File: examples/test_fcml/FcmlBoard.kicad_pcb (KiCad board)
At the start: 2 copper layers, 139 x 123 mm, 160 parts

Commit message: Update FcmlBoard.kicad_pcb
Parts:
- moved cdone.package 58.0 mm to (-35.0, 135.0), turned to 0 degrees
- moved cdone.res 56.7 mm to (-35.0, 137.0)
- moved fpga.vio_cap2 27.5 mm to (-35.0, 123.0), turned to 180 degrees
- moved fpga.vpp_cap 24.7 mm to (-21.0, 135.0)
- moved fpga.pll_hf 24.5 mm to (-25.0, 135.0)
- moved fpga.vio_cap1 20.5 mm to (-21.0, 137.0)
- moved fpga.pll_lf 20.2 mm to (-25.0, 139.0)
- moved fpga.vcc_cap 19.5 mm to (-35.0, 125.0), turned to 180 degrees
- moved fpga.vio_cap0 18.3 mm to (-25.0, 125.0), turned to 180 degrees
- moved fpga.reset_pu 16.5 mm to (-39.2, 151.0)
- moved fpga.pll_res 15.8 mm to (-25.0, 137.0), turned to 180 degrees
- moved fpga.mem_pu 6.42 mm to (-33.0, 154.0)

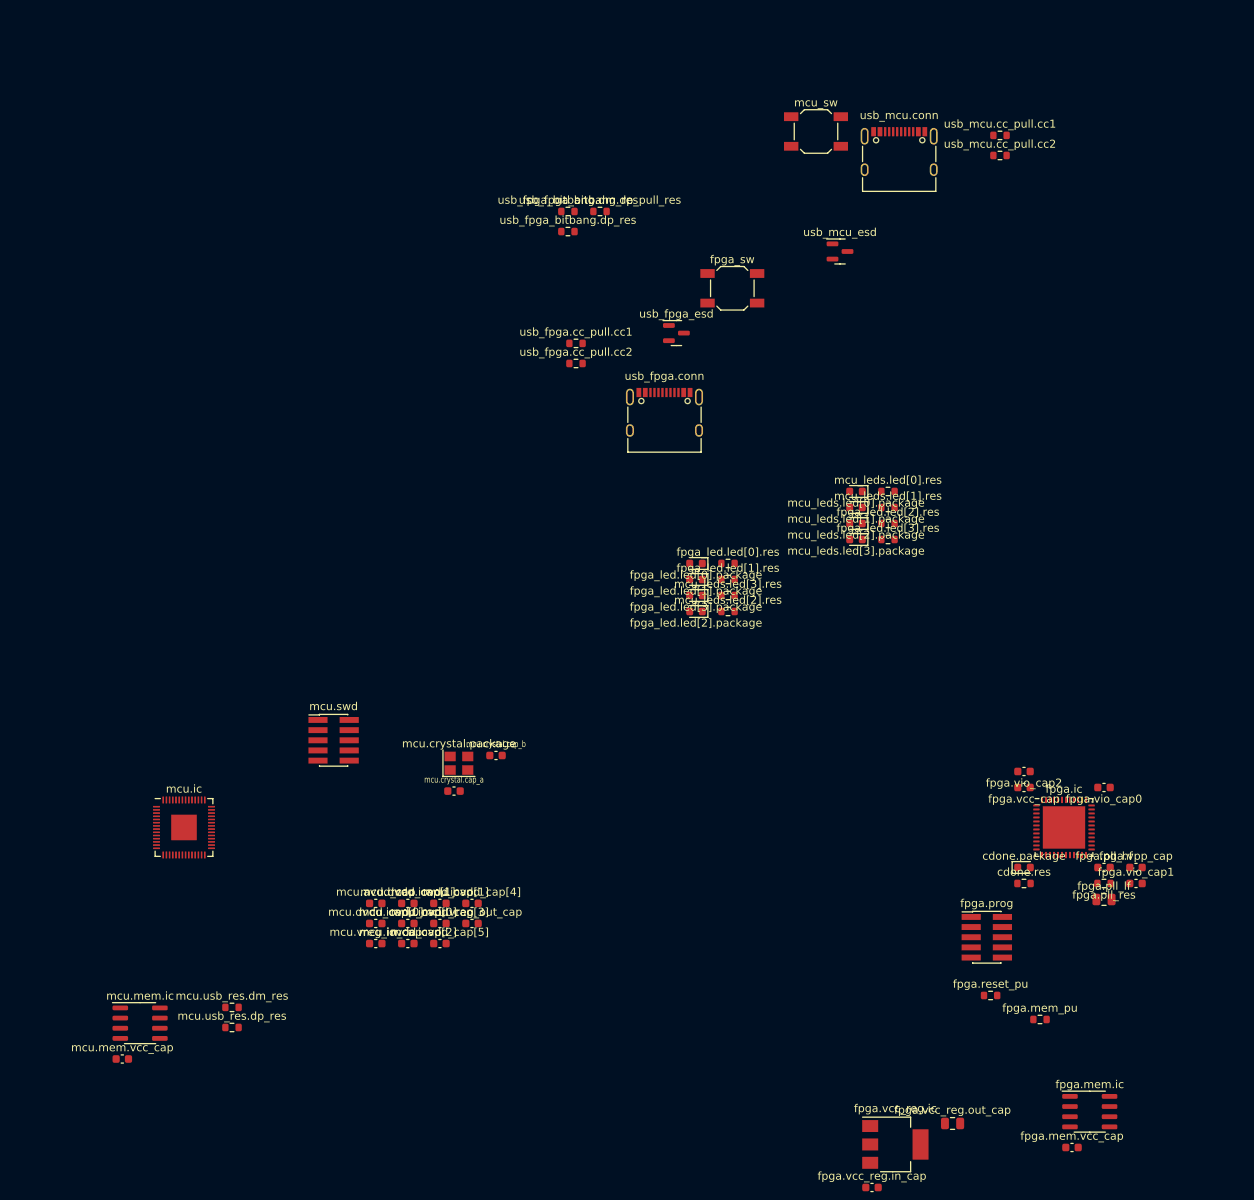
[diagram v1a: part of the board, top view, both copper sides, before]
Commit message: fpga and micro subckt routing
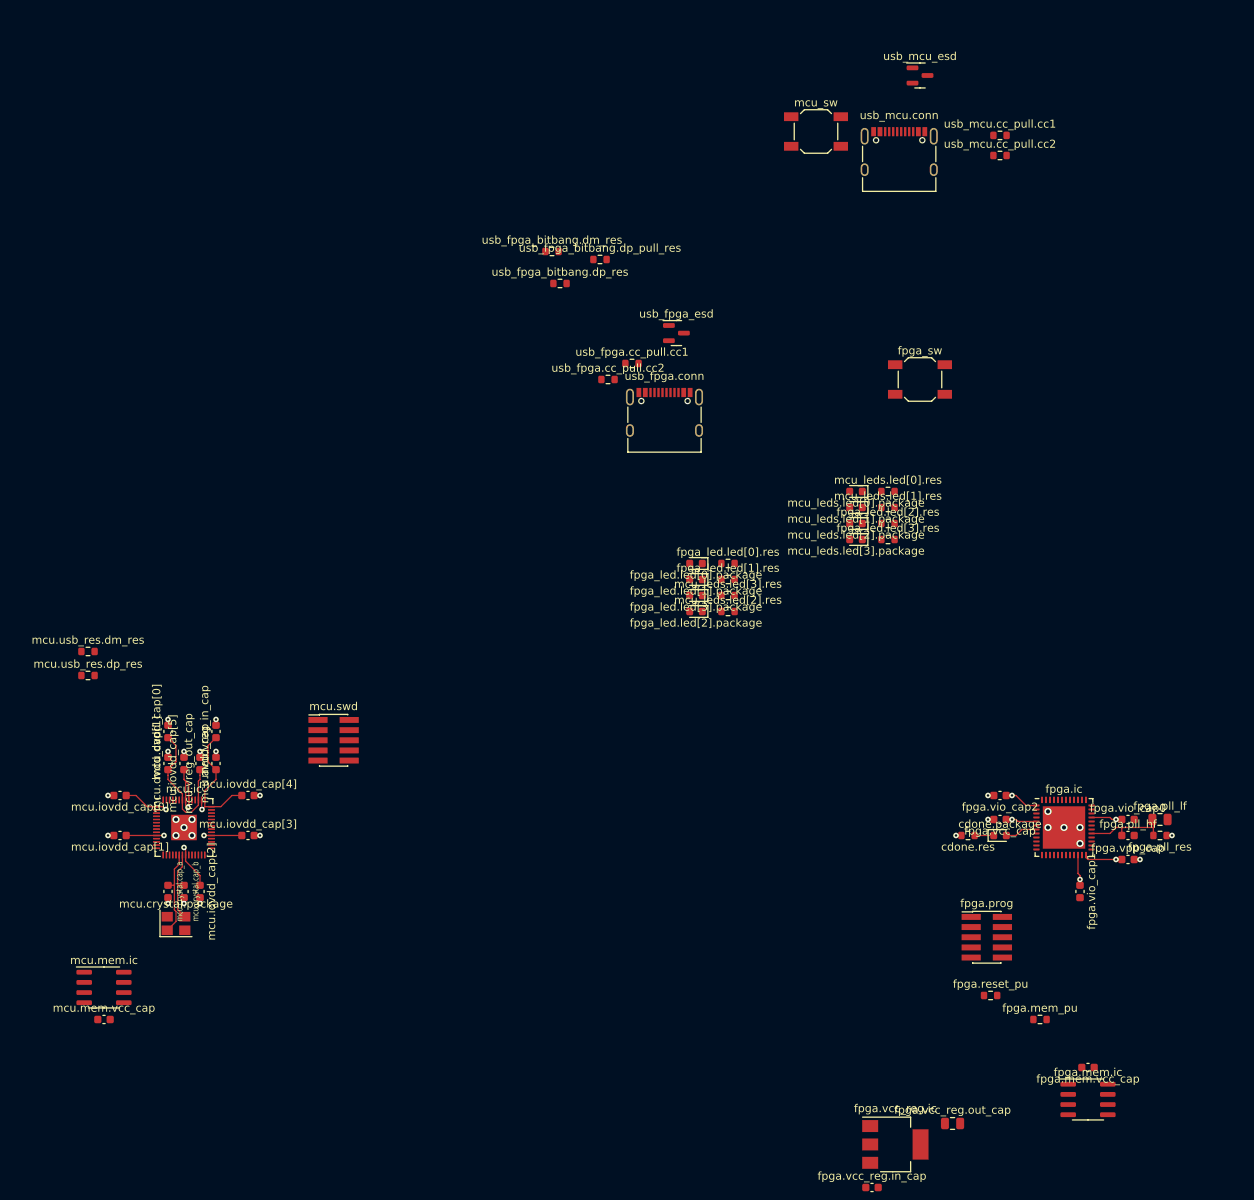
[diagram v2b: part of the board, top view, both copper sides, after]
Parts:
- moved mcu.usb_res.dm_res 48.0 mm to (-152.0, 108.0)
- moved mcu.usb_res.dp_res 47.5 mm to (-152.0, 111.0)
- moved mcu.crystal.cap_b 42.5 mm to (-140.0, 138.0), turned to -90 degrees
- moved mcu.iovdd_cap[1] 40.9 mm to (-148.0, 131.0), turned to 180 degrees
- moved mcu.crystal.package 40.6 mm to (-141.0, 142.0)
- moved mcu.vreg_out_cap 39.4 mm to (-138.0, 122.0), turned to 90 degrees
- moved mcu.iovdd_cap[0] 39.4 mm to (-148.0, 126.0), turned to 180 degrees
- moved mcu.iovdd_cap[5] 39.1 mm to (-140.0, 122.0), turned to 90 degrees
- moved mcu.crystal.cap_a 37.9 mm to (-142.0, 138.0), turned to -90 degrees
- moved mcu.dvdd_cap[0] 35.4 mm to (-142.0, 118.0), turned to 90 degrees
- moved mcu.dvdd_cap[1] 34.7 mm to (-142.0, 122.0), turned to 90 degrees
- moved mcu.vreg_in_cap 33.2 mm to (-136.0, 118.0), turned to 90 degrees
- moved mcu.iovdd_cap[4] 31.1 mm to (-132.0, 126.0)
- moved mcu.iovdd_cap[2] 26.8 mm to (-138.0, 138.0), turned to -90 degrees
- moved mcu.avdd_cap 26.5 mm to (-136.0, 122.0), turned to 90 degrees
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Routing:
- net v3v3: track 45.7 -> 110.4 mm, vias 4 -> 14
- net gnd: track 30.5 -> 58.1 mm, vias 22 -> 49
- net mcu.ic.vreg_vout: track 0.00 -> 17.5 mm
- net fpga.pll_res.pwr_out: track 0.00 -> 11.1 mm
- net mcu.crystal.crystal.a: track 0.00 -> 11.0 mm
- net mcu.crystal.crystal.b: track 0.00 -> 9.14 mm
- net fpga.vcc_reg.pwr_out: track 0.00 -> 5.28 mm, vias 0 -> 2
- net fpga.cdone: track 0.00 -> 4.07 mm
- net cdone.res.a: track 0.00 -> 2.39 mm

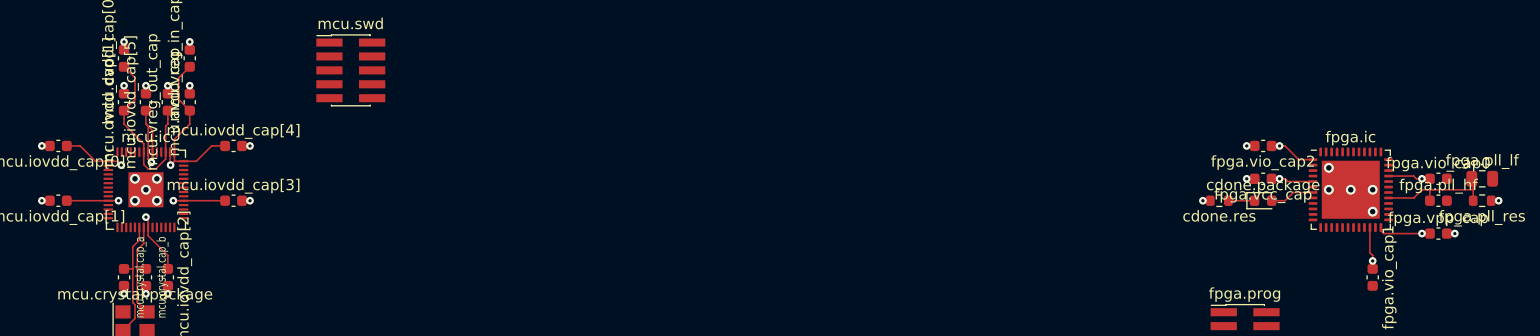
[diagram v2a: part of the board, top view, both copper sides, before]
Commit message: thicker power traces
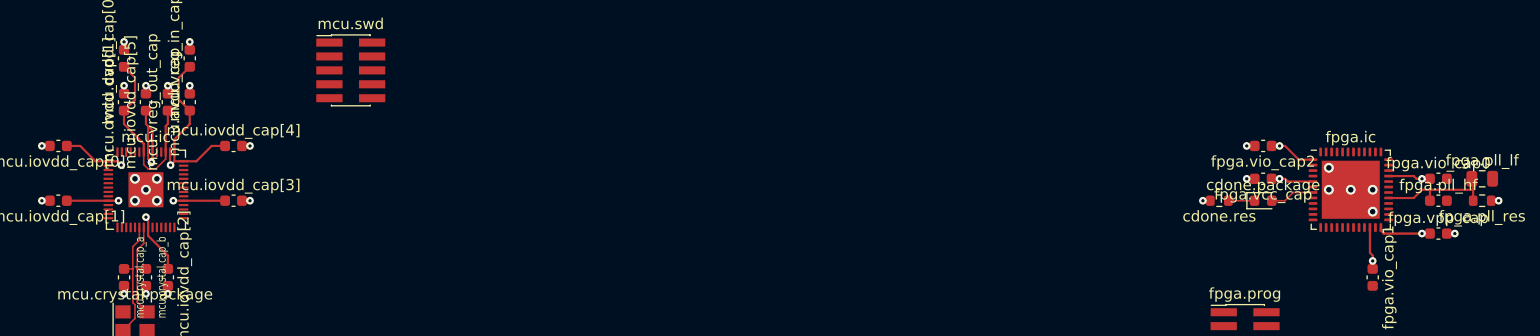
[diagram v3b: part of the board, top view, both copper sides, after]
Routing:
- net fpga.pll_res.pwr_out: track 11.1 -> 17.6 mm
- net v3v3: track 110.4 -> 116.4 mm

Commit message: Update FcmlBoard.kicad_pcb
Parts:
- moved reg_3v3.ic 197.6 mm to (-106.3, 75.4)
- moved reg_3v3.in_cap 197.6 mm to (-99.4, 72.5)
- moved reg_3v3.out_cap 197.6 mm to (-109.0, 81.0)
- moved mcu_sw 91.3 mm to (-136.0, 95.0)
- moved fpga_sw 34.2 mm to (-27.0, 101.0)
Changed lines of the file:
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@@
   )
   (footprint "Button_Switch_SMD:SW_SPST_SKQG_WithoutStem" (layer "F.Cu")
-    (at -48 74)
+    (at -27 101)
     (descr "ALPS 5.2mm Square Low-profile Type (Surface Mount) SKQG Series, Without stem, http://www.alps.com/prod/info/E/HTML/Tact/SurfaceMount/SKQG/SKQGAEE010.html")
     (tags "SPST Button Switch")
@@
       (polygon
         (pts
-          (xy -47 72.7)
-          (xy -44 72.7)
-          (xy -44 75.3)
-          (xy -47 75.3)
+          (xy -26 99.7)
+          (xy -23 99.7)
+          (xy -23 102.3)
+          (xy -26 102.3)
         )
       )
@@
       (polygon
         (pts
-          (xy -52 72.7)
-          (xy -49 72.7)
-          (xy -49 75.3)
-          (xy -52 75.3)
+          (xy -31 99.7)
+          (xy -28 99.7)
+          (xy -28 102.3)
+          (xy -31 102.3)
         )
       )
@@
   )
   (footprint "Capacitor_SMD:C_0805_2012Metric" (layer "F.Cu")
-    (at 81.07 27.14)
+    (at -109 81)
     (descr "Capacitor SMD 0805 (2012 Metric), square (rectangular) end terminal, IPC_7351 nominal, (Body size source: IPC-SM-782 page 76, https://www.pcb-3d.com/wordpress/wp-content/uploads/ipc-sm-782a_amendment_1_and_2.pdf, https://docs.google.com/spreadsheets/d/1BsfQQcO9C6DZCsRaXUlFlo91Tg2WpOkGARC1WS5S8t0/edit?usp=sharing), generated with kicad-footprint-generator")
     (tags "capacitor")
@@
   )
   (footprint "Package_TO_SOT_SMD:SOT-223-3_TabPin2" (layer "F.Cu")
-    (at 83.77 21.51)
+    (at -106.3 75.37)
     (descr "module CMS SOT223 4 pins")
     (tags "CMS SOT")
@@
   )
   (footprint "Capacitor_SMD:C_0603_1608Metric" (layer "F.Cu")
-    (at 90.7 18.64)
+    (at -99.37 72.5)
     (descr "Capacitor SMD 0603 (1608 Metric), square (rectangular) end terminal, IPC_7351 nominal, (Body size source: IPC-SM-782 page 76, https://www.pcb-3d.com/wordpress/wp-content/uploads/ipc-sm-782a_amendment_1_and_2.pdf), generated with kicad-footprint-generator")
     (tags "capacitor")
@@
   )
   (footprint "Button_Switch_SMD:SW_SPST_SKQG_WithoutStem" (layer "F.Cu")
-    (at -61 43)
+    (at -136 95)
     (descr "ALPS 5.2mm Square Low-profile Type (Surface Mount) SKQG Series, Without stem, http://www.alps.com/prod/info/E/HTML/Tact/SurfaceMount/SKQG/SKQGAEE010.html")
     (tags "SPST Button Switch")
@@
       (polygon
         (pts
-          (xy -60 41.7)
-          (xy -57 41.7)
-          (xy -57 44.3)
-          (xy -60 44.3)
+          (xy -135 93.7)
+          (xy -132 93.7)
+          (xy -132 96.3)
+          (xy -135 96.3)
         )
       )
@@
       (polygon
         (pts
-          (xy -65 41.7)
-          (xy -62 41.7)
-          (xy -62 44.3)
-          (xy -65 44.3)
+          (xy -140 93.7)
+          (xy -137 93.7)
+          (xy -137 96.3)
+          (xy -140 96.3)
         )
       )

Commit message: Update FcmlBoard.kicad_pcb
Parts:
- moved mcu.mem.vcc_cap 46.3 mm to (-139.0, 109.0), turned to 180 degrees
- moved mcu.mem.ic 38.6 mm to (-139.0, 113.0)
- moved fpga.prog 29.4 mm to (-23.0, 168.0)
- moved fpga.mem.ic 21.2 mm to (-30.0, 143.0), turned to 180 degrees
- moved fpga.mem.vcc_cap 13.3 mm to (-30.0, 147.0), turned to 0 degrees
- moved mcu.dvdd_cap[0] 2.00 mm to (-140.0, 118.0)
- moved mcu.vreg_in_cap 2.00 mm to (-138.0, 118.0)
- moved conv.power_path.inductor 1.00 mm to (90.0, 111.0)
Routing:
- net conv.sw[2].low_boot_out: track 55.5 -> 58.5 mm
- net gnd: track 58.1 -> 59.9 mm, vias 49 -> 51
